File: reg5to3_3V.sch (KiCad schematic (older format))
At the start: 3 parts

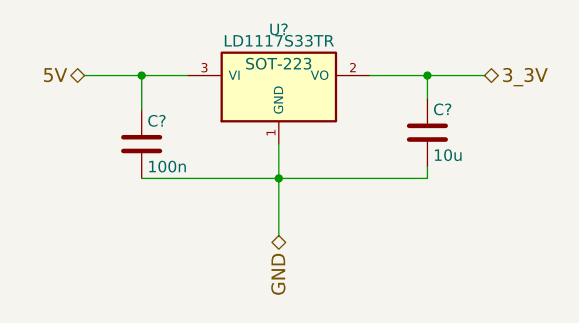
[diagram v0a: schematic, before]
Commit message: resueltos probelams con duplicados y checkeado esquematico
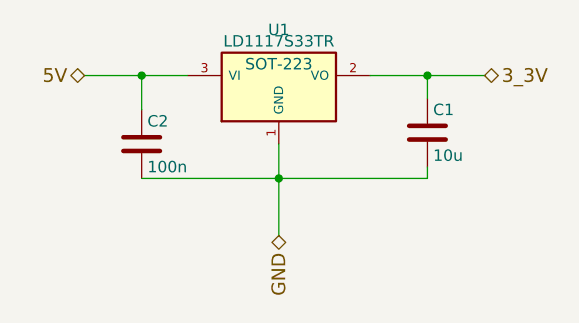
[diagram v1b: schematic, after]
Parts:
- gave numbers to parts that had none: 3
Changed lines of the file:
@@
 $EndDescr
 $Comp
-L LD1117S33TR U?
+L LD1117S33TR U1
 U 1 1 57126C2F
 P 4700 2800
-F 0 "U?" H 4700 3050 50  0000 C CNN
+F 0 "U1" H 4700 3050 50  0000 C CNN
 F 1 "LD1117S33TR" H 4700 3000 50  0000 C CNN
 F 2 "SOT-223" H 4700 2900 50  0000 C CNN
@@
 $EndComp
 $Comp
-L C C?
+L C C2
 U 1 1 57126C5D
 P 4100 3050
-F 0 "C?" H 4125 3150 50  0000 L CNN
+F 0 "C2" H 4125 3150 50  0000 L CNN
 F 1 "100n" H 4125 2950 50  0000 L CNN
 F 2 "" H 4138 2900 50  0000 C CNN
@@
 $EndComp
 $Comp
-L C C?
+L C C1
 U 1 1 57126C91
 P 5350 3000
-F 0 "C?" H 5375 3100 50  0000 L CNN
+F 0 "C1" H 5375 3100 50  0000 L CNN
 F 1 "10u" H 5375 2900 50  0000 L CNN
 F 2 "" H 5388 2850 50  0000 C CNN

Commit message: intento de asginar huellas
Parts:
- U1: footprint SOT-223 -> TO_SOT_Packages_SMD:SOT-223
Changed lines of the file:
@@
 F 0 "U1" H 4700 3050 50  0000 C CNN
 F 1 "LD1117S33TR" H 4700 3000 50  0000 C CNN
-F 2 "SOT-223" H 4700 2900 50  0000 C CNN
+F 2 "TO_SOT_Packages_SMD:SOT-223" H 4700 2900 50  0000 C CNN
 F 3 "" H 4700 2800 50  0000 C CNN
 	1    4700 2800
@@
 F 0 "C2" H 4125 3150 50  0000 L CNN
 F 1 "100n" H 4125 2950 50  0000 L CNN
-F 2 "" H 4138 2900 50  0000 C CNN
+F 2 "" H 4138 2900 50  0001 C CNN
 F 3 "" H 4100 3050 50  0000 C CNN
 	1    4100 3050
@@
 F 0 "C1" H 5375 3100 50  0000 L CNN
 F 1 "10u" H 5375 2900 50  0000 L CNN
-F 2 "" H 5388 2850 50  0000 C CNN
+F 2 "" H 5388 2850 50  0001 C CNN
 F 3 "" H 5350 3000 50  0000 C CNN
 	1    5350 3000

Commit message: nuevo componente diseñado L293DD, asignadas huellas
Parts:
- C1, C2: footprint (none) -> Capacitors_SMD:C_0402
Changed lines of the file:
@@
 F 0 "C2" H 4125 3150 50  0000 L CNN
 F 1 "100n" H 4125 2950 50  0000 L CNN
-F 2 "" H 4138 2900 50  0001 C CNN
+F 2 "Capacitors_SMD:C_0402" H 4138 2900 50  0001 C CNN
 F 3 "" H 4100 3050 50  0000 C CNN
 	1    4100 3050
@@
 F 0 "C1" H 5375 3100 50  0000 L CNN
 F 1 "10u" H 5375 2900 50  0000 L CNN
-F 2 "" H 5388 2850 50  0001 C CNN
+F 2 "Capacitors_SMD:C_0402" H 5388 2850 50  0001 C CNN
 F 3 "" H 5350 3000 50  0000 C CNN
 	1    5350 3000

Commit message: actualizaciones en CRM. TODO: cambiar L293DD por L298smd, cambiar para controlar ENs con pwm, y pines de direccion de motores desde el extensor de pines, eliminar jumpers, ajustar tamaño de las resistencias
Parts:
- C1, C2: footprint Capacitors_SMD:C_0402 -> Capacitors_SMD:C_1825_HandSoldering
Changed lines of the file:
@@
 F 0 "C2" H 4125 3150 50  0000 L CNN
 F 1 "100n" H 4125 2950 50  0000 L CNN
-F 2 "Capacitors_SMD:C_0402" H 4138 2900 50  0001 C CNN
+F 2 "Capacitors_SMD:C_1825_HandSoldering" H 4138 2900 50  0001 C CNN
 F 3 "" H 4100 3050 50  0000 C CNN
 	1    4100 3050
@@
 F 0 "C1" H 5375 3100 50  0000 L CNN
 F 1 "10u" H 5375 2900 50  0000 L CNN
-F 2 "Capacitors_SMD:C_0402" H 5388 2850 50  0001 C CNN
+F 2 "Capacitors_SMD:C_1825_HandSoldering" H 5388 2850 50  0001 C CNN
 F 3 "" H 5350 3000 50  0000 C CNN
 	1    5350 3000

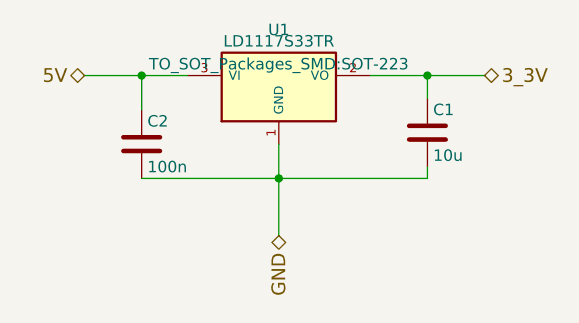
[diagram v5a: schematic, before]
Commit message: autorouting generado con freerouting
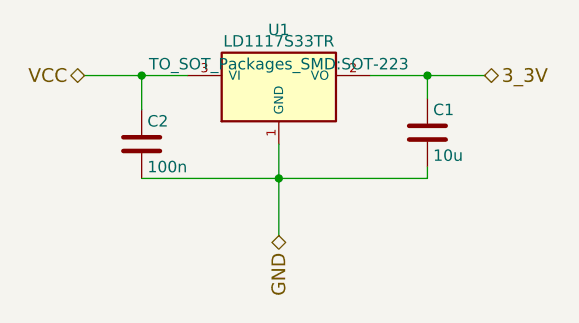
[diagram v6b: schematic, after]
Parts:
- C1, C2: footprint Capacitors_SMD:C_1825_HandSoldering -> Capacitors_SMD:C_0805_HandSoldering
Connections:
- net 5V renamed VCC
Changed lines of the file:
@@
 F 0 "C2" H 4125 3150 50  0000 L CNN
 F 1 "100n" H 4125 2950 50  0000 L CNN
-F 2 "Capacitors_SMD:C_1825_HandSoldering" H 4138 2900 50  0001 C CNN
+F 2 "Capacitors_SMD:C_0805_HandSoldering" H 4138 2900 50  0001 C CNN
 F 3 "" H 4100 3050 50  0000 C CNN
 	1    4100 3050
@@
 F 0 "C1" H 5375 3100 50  0000 L CNN
 F 1 "10u" H 5375 2900 50  0000 L CNN
-F 2 "Capacitors_SMD:C_1825_HandSoldering" H 5388 2850 50  0001 C CNN
+F 2 "Capacitors_SMD:C_0805_HandSoldering" H 5388 2850 50  0001 C CNN
 F 3 "" H 5350 3000 50  0000 C CNN
 	1    5350 3000
@@
 Connection ~ 4100 2750
 Text HLabel 3850 2750 0    60   BiDi ~ 0
-5V
+VCC
 Wire Wire Line
 	5100 2750 5600 2750

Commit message: cambio de posiciones en la placa
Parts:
- C1, C2: footprint Capacitors_SMD:C_0805_HandSoldering -> Capacitors_SMD:C_1206
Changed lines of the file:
@@
 F 0 "C2" H 4125 3150 50  0000 L CNN
 F 1 "100n" H 4125 2950 50  0000 L CNN
-F 2 "Capacitors_SMD:C_0805_HandSoldering" H 4138 2900 50  0001 C CNN
+F 2 "Capacitors_SMD:C_1206" H 4138 2900 50  0001 C CNN
 F 3 "" H 4100 3050 50  0000 C CNN
 	1    4100 3050
@@
 F 0 "C1" H 5375 3100 50  0000 L CNN
 F 1 "10u" H 5375 2900 50  0000 L CNN
-F 2 "Capacitors_SMD:C_0805_HandSoldering" H 5388 2850 50  0001 C CNN
+F 2 "Capacitors_SMD:C_1206" H 5388 2850 50  0001 C CNN
 F 3 "" H 5350 3000 50  0000 C CNN
 	1    5350 3000
